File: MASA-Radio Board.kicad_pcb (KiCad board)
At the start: 2 copper layers, 75.8 x 76.2 mm, 22 parts, among them IC1 FAN4010IL6X_F113, J1 SC_19-20, U1 MP5077GG-Z, U3 BL654PA, U5 MCP2515-xSO, U6 SN65HVD1050D

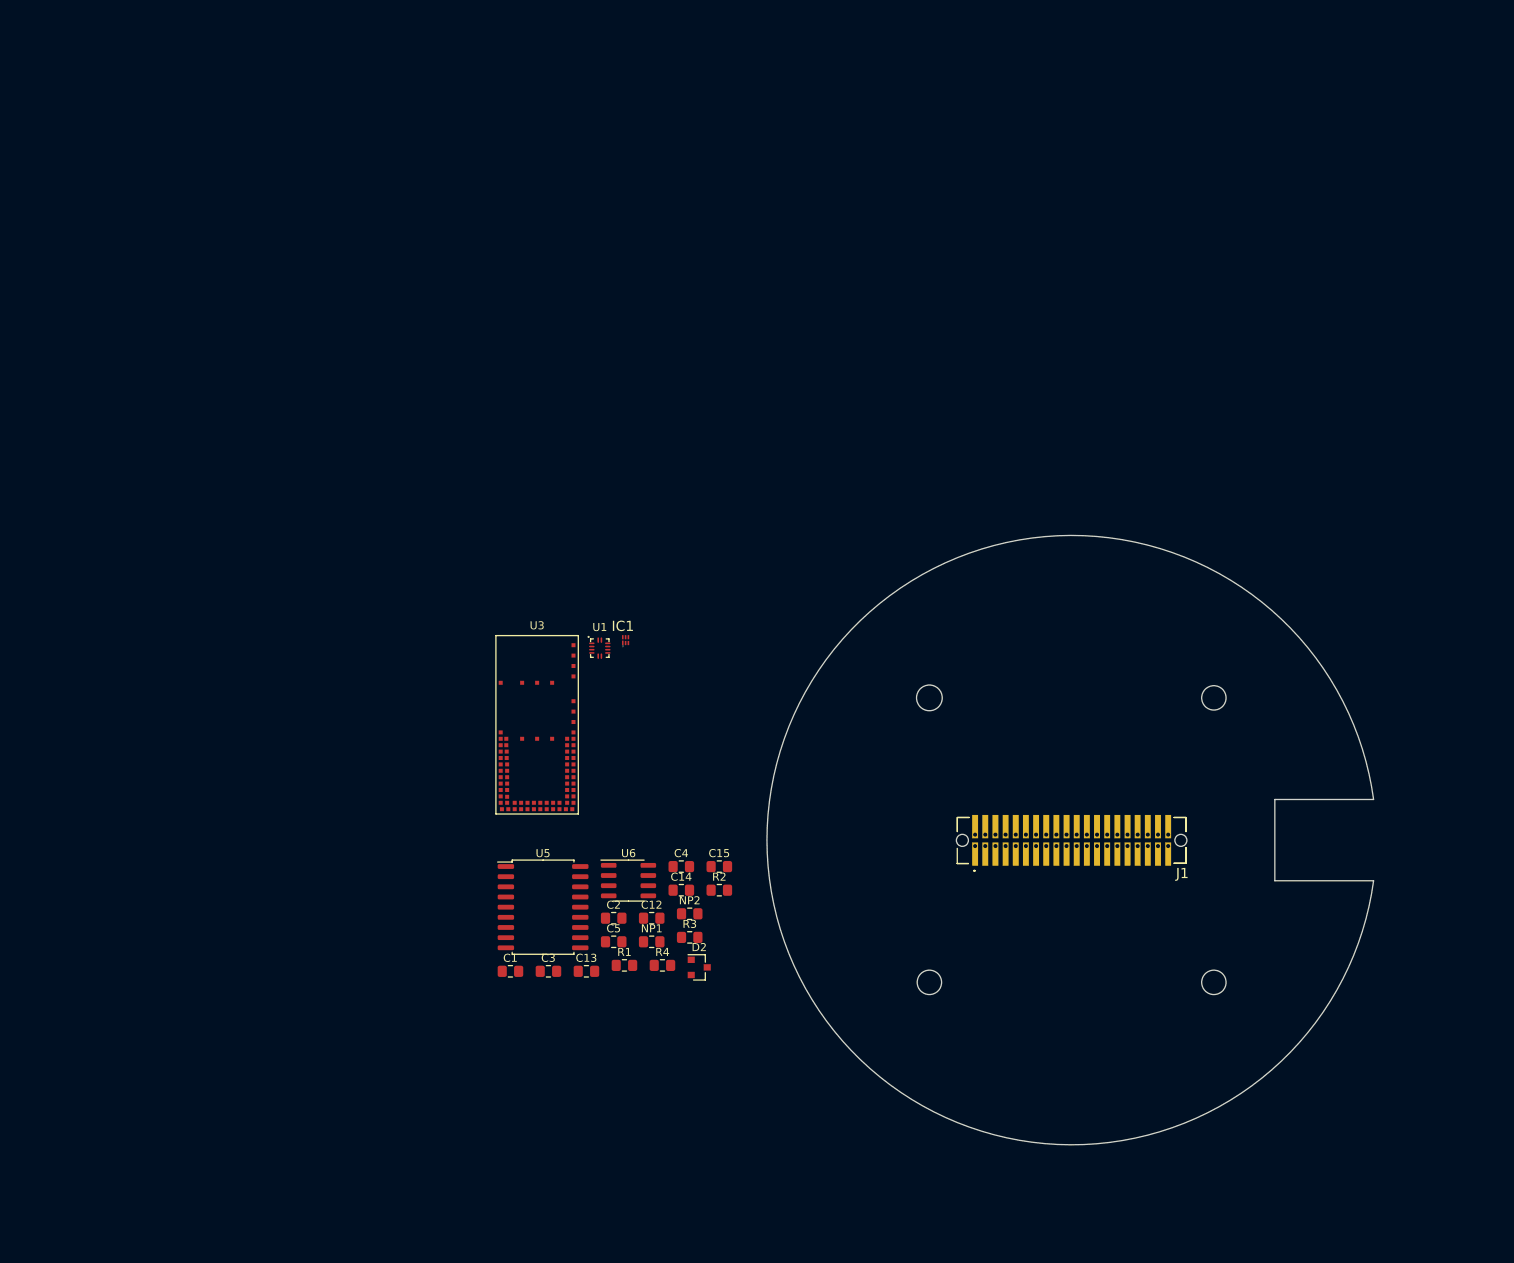
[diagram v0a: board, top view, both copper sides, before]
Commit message: Some minor footprint and value updates - unfinished
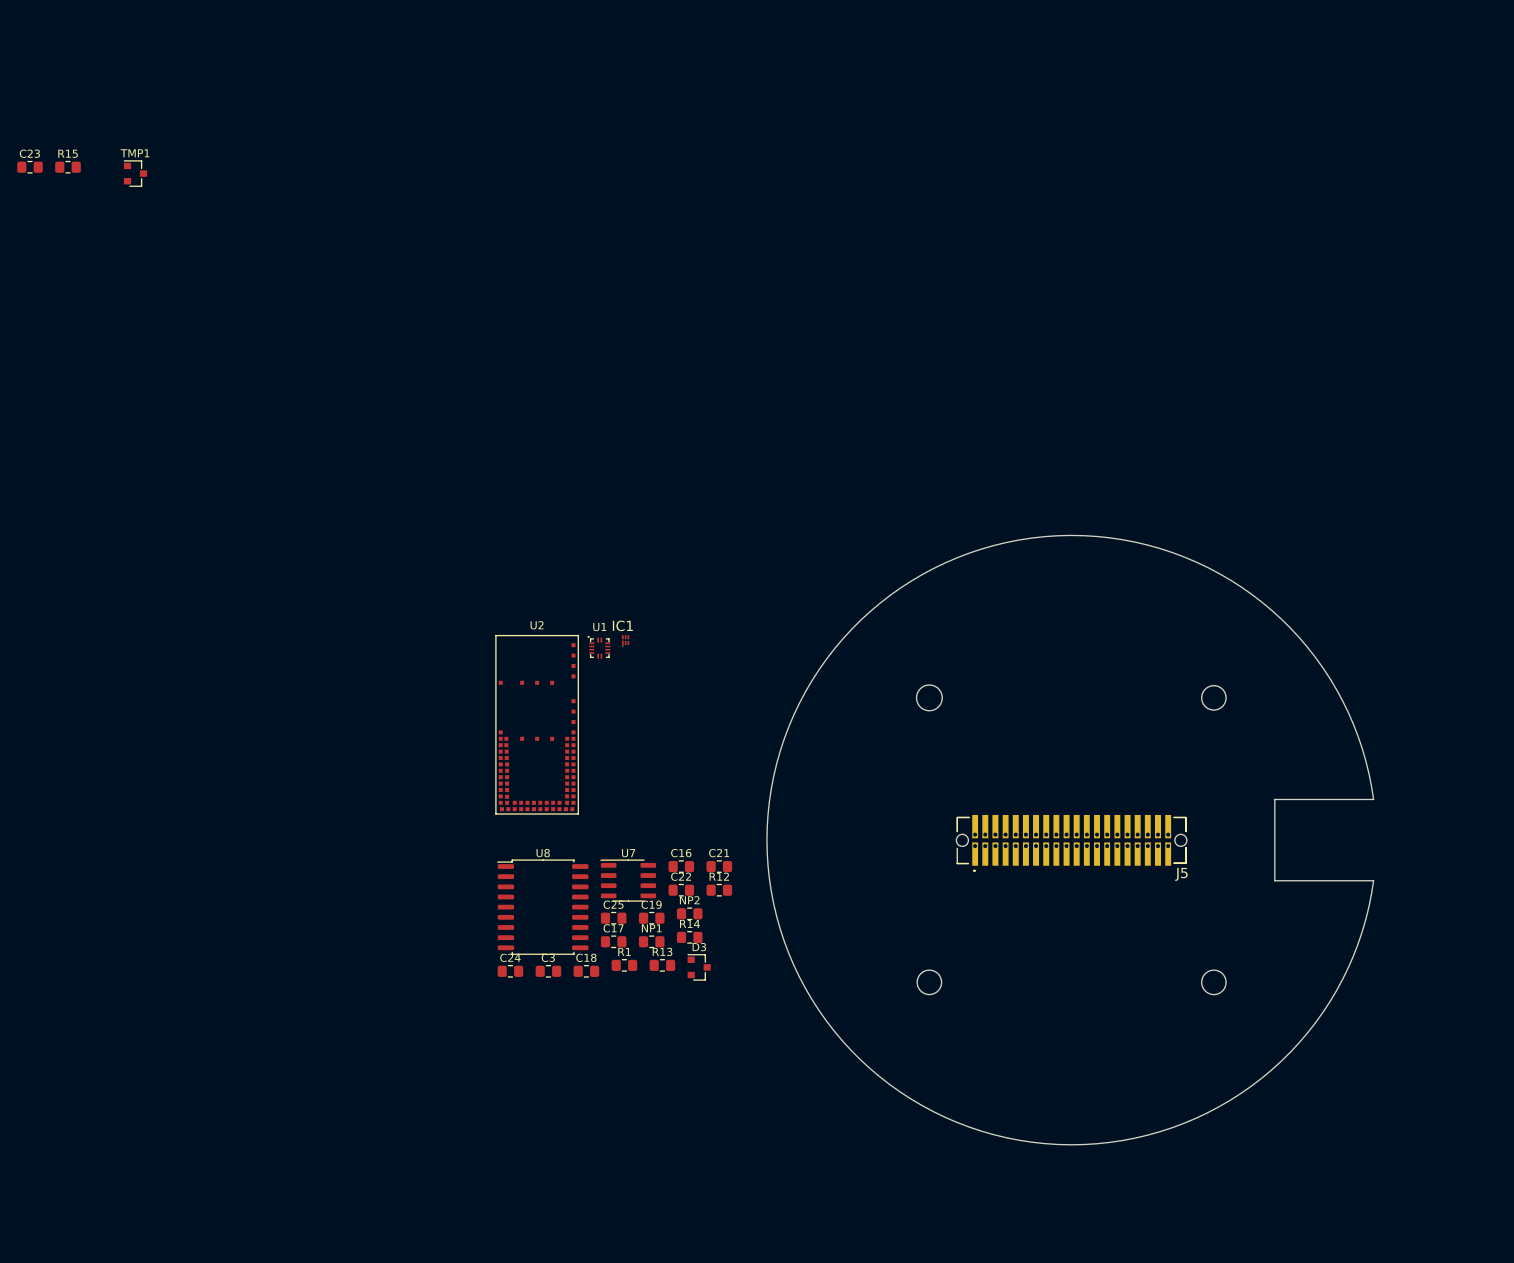
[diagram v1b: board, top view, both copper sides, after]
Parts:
- added C23: 100pf, Capacitor_SMD:C_0805_2012Metric_Pad1.15x1.40mm_HandSolder, F.Cu at (22.2, 42.9)
- added R15: 0, Resistor_SMD:R_0805_2012Metric_Pad1.15x1.40mm_HandSolder, F.Cu at (26.9, 42.9)
- added TMP1: LM50CIM3X, Package_TO_SOT_SMD:SOT-23, F.Cu at (35.4, 43.7)
- renumbered C4 to C16, C5 to C17, C13 to C18, C12 to C19, C15 to C21, C14 to C22, C1 to C24, C2 to C25, D2 to D3, J1 to J5, R2 to R12, R4 to R13, R3 to R14, U3 to U2, U6 to U7, U5 to U8
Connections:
- net Net-(U3-Pad15) renamed USB_D+
- net Net-(U3-Pad17) renamed USB_D-
- net Net-(U3-Pad5) renamed nAutoRun
- net UART1_RX renamed XBee_TX
- net UART1_TX renamed Net-(J5-Pad25)
- C16 pad 1: GND -> Net-(C16-Pad1)
- C16 pad 2: Net-(C4-Pad2) -> GND
- C24 pad 1: +5V -> +3V3
- C25 pad 2: +5V -> +3V3
- R12 pad 1: Net-(C4-Pad2) -> Net-(C16-Pad1)
- U1 pad 5: Net-(C10-Pad1) -> Net-(C3-Pad1)
- U2 pad 24: +5V -> USB_VBUS
- U7 pad 1: Net-(C4-Pad2) -> Net-(C20-Pad2)
- U7 pad 4: Net-(R1-Pad2) -> Net-(R15-Pad1)
- U8 pad 2: Net-(C3-Pad1) -> Net-(U8-Pad2)
- U8 pad 9: +5V -> +3V3

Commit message: Updated footprints, began board layout, board layers
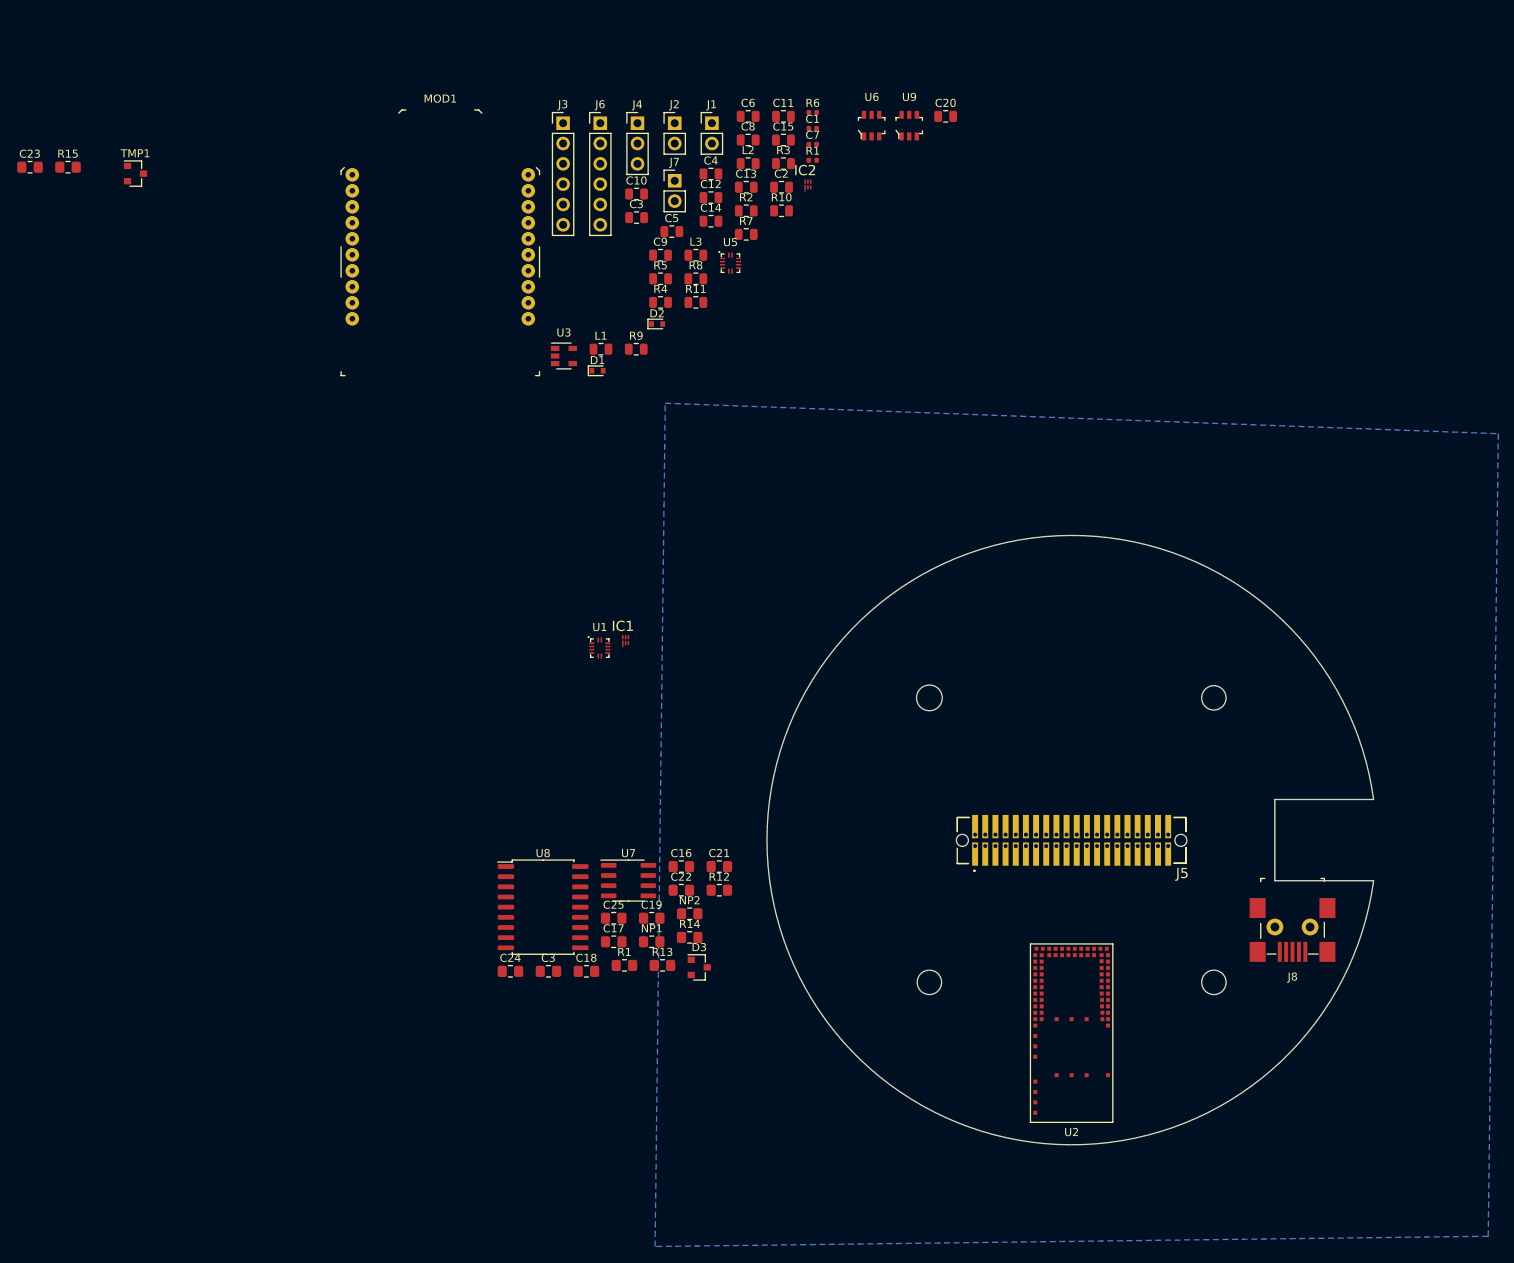
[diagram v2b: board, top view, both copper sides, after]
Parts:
- added C1: 10nF, Capacitor_SMD:C_0402_1005Metric, F.Cu at (120.0, 38.0)
- added C10: 100nF, Capacitor_SMD:C_0805_2012Metric, F.Cu at (98.0, 46.2)
- added C11: 100nF, Capacitor_SMD:C_0805_2012Metric, F.Cu at (116.4, 36.5)
- added C12: 1nF, Capacitor_SMD:C_0805_2012Metric, F.Cu at (107.3, 46.7)
- added C13: 100nF, Capacitor_SMD:C_0805_2012Metric, F.Cu at (111.7, 45.4)
- added C14: 2.2uF, Capacitor_SMD:C_0805_2012Metric, F.Cu at (107.3, 49.6)
- added C15: 1uF, Capacitor_SMD:C_0805_2012Metric, F.Cu at (116.4, 39.5)
- added C2: 22uF, Capacitor_SMD:C_0805_2012Metric, F.Cu at (116.1, 45.4)
- added C20: 100pF, Capacitor_SMD:C_0805_2012Metric, F.Cu at (136.7, 36.5)
- added C3: 0.68uF, Capacitor_SMD:C_0805_2012Metric, F.Cu at (98.0, 49.2)
- added C4: 1uF, Capacitor_SMD:C_0805_2012Metric, F.Cu at (107.3, 43.7)
- added C5: 1uF, Capacitor_SMD:C_0805_2012Metric, F.Cu at (102.4, 50.9)
- added C6: 4.7uF, Capacitor_SMD:C_0805_2012Metric, F.Cu at (112.0, 36.5)
- added C7: 10nF, Capacitor_SMD:C_0402_1005Metric, F.Cu at (120.0, 40.0)
- added C8: 22nF, Capacitor_SMD:C_0805_2012Metric, F.Cu at (112.0, 39.5)
- added C9: 1nF, Capacitor_SMD:C_0805_2012Metric, F.Cu at (101.0, 53.9)
- added D1: D_TVS, Diode_SMD:D_SOD-523, F.Cu at (93.1, 68.3)
- added D2: D_TVS, Diode_SMD:D_SOD-523, F.Cu at (100.6, 62.5)
- added IC2: FAN4010IL6X_F113, MASA_Library:6-LEAD_MICROPAK, F.Cu at (119.4, 45.0)
- added J1: Conn_01x02, Connector_PinHeader_2.54mm:PinHeader_1x02_P2.54mm_Vertical, F.Cu at (107.4, 37.4)
- added J2: Conn_01x02_Male, Connector_PinHeader_2.54mm:PinHeader_1x02_P2.54mm_Vertical, F.Cu at (102.8, 37.4)
- added J3: Conn_01x06, Connector_PinHeader_2.54mm:PinHeader_1x06_P2.54mm_Vertical, F.Cu at (88.8, 37.4)
- added J4: Conn_01x03_Male, Connector_PinHeader_2.54mm:PinHeader_1x03_P2.54mm_Vertical, F.Cu at (98.1, 37.4)
- added J6: Conn_01x06, Connector_PinHeader_2.54mm:PinHeader_1x06_P2.54mm_Vertical, F.Cu at (93.5, 37.4)
- added J7: Conn_01x02, Connector_PinHeader_2.54mm:PinHeader_1x02_P2.54mm_Vertical, F.Cu at (102.8, 44.6)
- added J8: UJ2-MBH-1-SMT-TR, digikey-footprints:USB_Mini_B_Female_UJ2-MBH-1-SMT-TR, F.Cu at (180.0, 133.1)
- added L1: 4.7uH, Inductor_SMD:L_0805_2012Metric, F.Cu at (93.6, 65.6)
- added L2: 4.7uH, Inductor_SMD:L_0805_2012Metric, F.Cu at (112.0, 42.4)
- added L3: 2.2u, Inductor_SMD:L_0805_2012Metric, F.Cu at (105.4, 53.9)
- added MOD1: XBP9B-DPST-001, digikey-footprints:XBEE_PRO-20_THT, F.Cu at (73.5, 52.8)
- added R1: 1, Resistor_SMD:R_0402_1005Metric, F.Cu at (120.0, 42.0)
- added R10: 3.3k, Resistor_SMD:R_0805_2012Metric, F.Cu at (116.1, 48.3)
- added R11: 3.3, Resistor_SMD:R_0805_2012Metric, F.Cu at (105.4, 59.8)
- added R2: 200k, Resistor_SMD:R_0805_2012Metric, F.Cu at (111.7, 48.3)
- added R3: 200m, Resistor_SMD:R_0805_2012Metric, F.Cu at (116.4, 42.4)
- added R4: 3k, Resistor_SMD:R_0805_2012Metric, F.Cu at (101.0, 59.8)
- added R5: 100k, Resistor_SMD:R_0805_2012Metric, F.Cu at (101.0, 56.8)
- added R6: 1, Resistor_SMD:R_0402_1005Metric, F.Cu at (120.0, 36.1)
- added R7: 1, Resistor_SMD:R_0805_2012Metric, F.Cu at (111.7, 51.3)
- added R8: 3k, Resistor_SMD:R_0805_2012Metric, F.Cu at (105.4, 56.8)
- added R9: 820k, Resistor_SMD:R_0805_2012Metric, F.Cu at (98.0, 65.6)
- added U3: MIC5504-3.3YM5, Package_TO_SOT_SMD:SOT-23-5, F.Cu at (88.9, 66.5)
- added U5: MP5077GG-Z, MASA_Library:MP5077GG-Z, F.Cu at (109.8, 54.9)
- added U6: SN74LVC1T45DBVR, digikey-footprints:SOT-23-6, F.Cu at (127.4, 37.7)
- added U9: SN74LVC1T45DBVR, digikey-footprints:SOT-23-6, F.Cu at (132.1, 37.7)
- moved U2 77.1 mm to (152.4, 151.1), turned to 180 degrees
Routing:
- added copper zone on B.Cu, net +3V3
- added copper zone on In1.Cu, net GND
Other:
- copper layers 2 -> 4
